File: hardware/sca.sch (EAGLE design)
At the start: 45 parts, among them Q1 BSS138, Q2 BSS138, U1 MIC5225-3.3, U5 FGPMMOPA6H, U6 MIC5225-3.3, Y1 32.768kHz

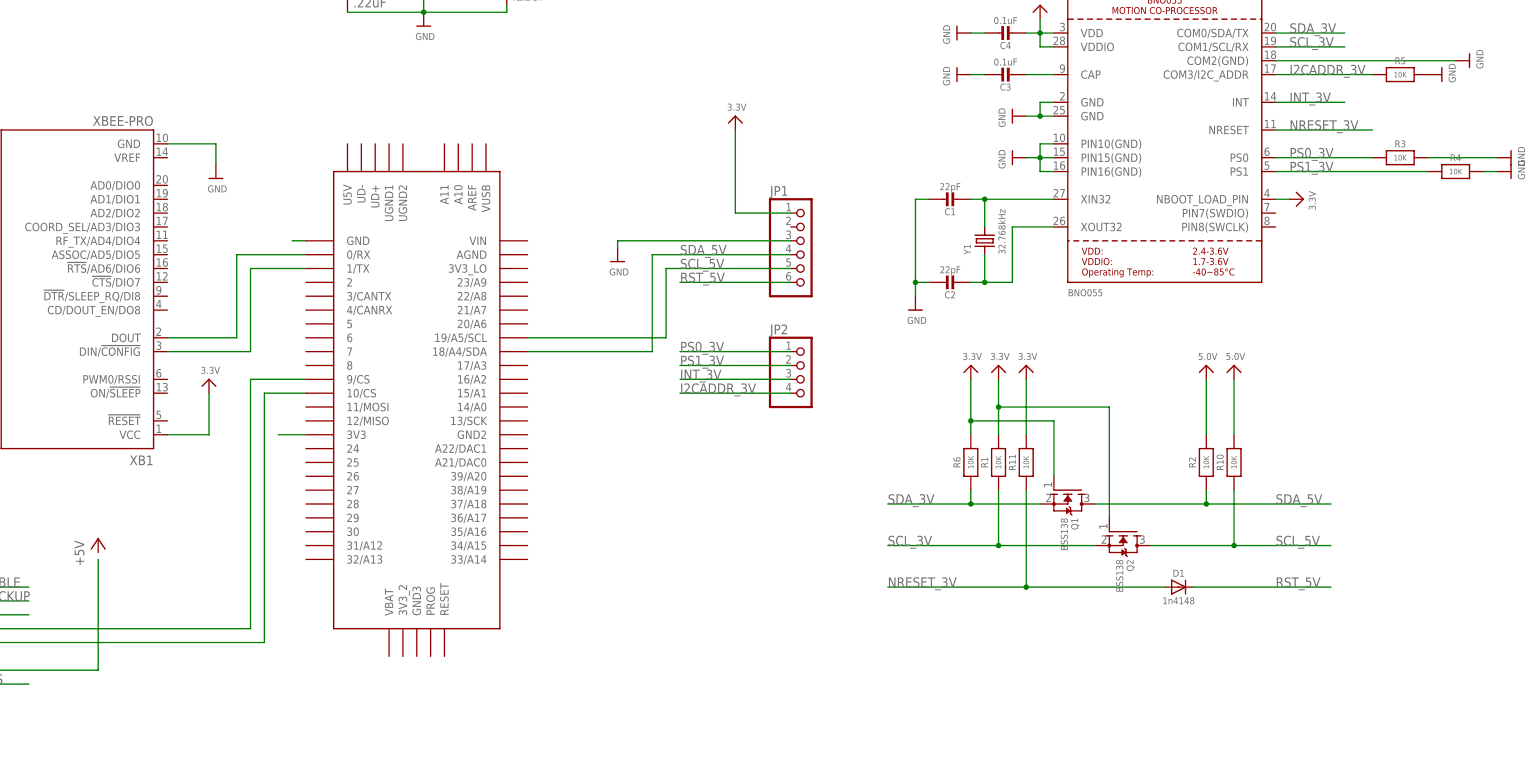
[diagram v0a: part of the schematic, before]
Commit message: Added 4x photoresistors
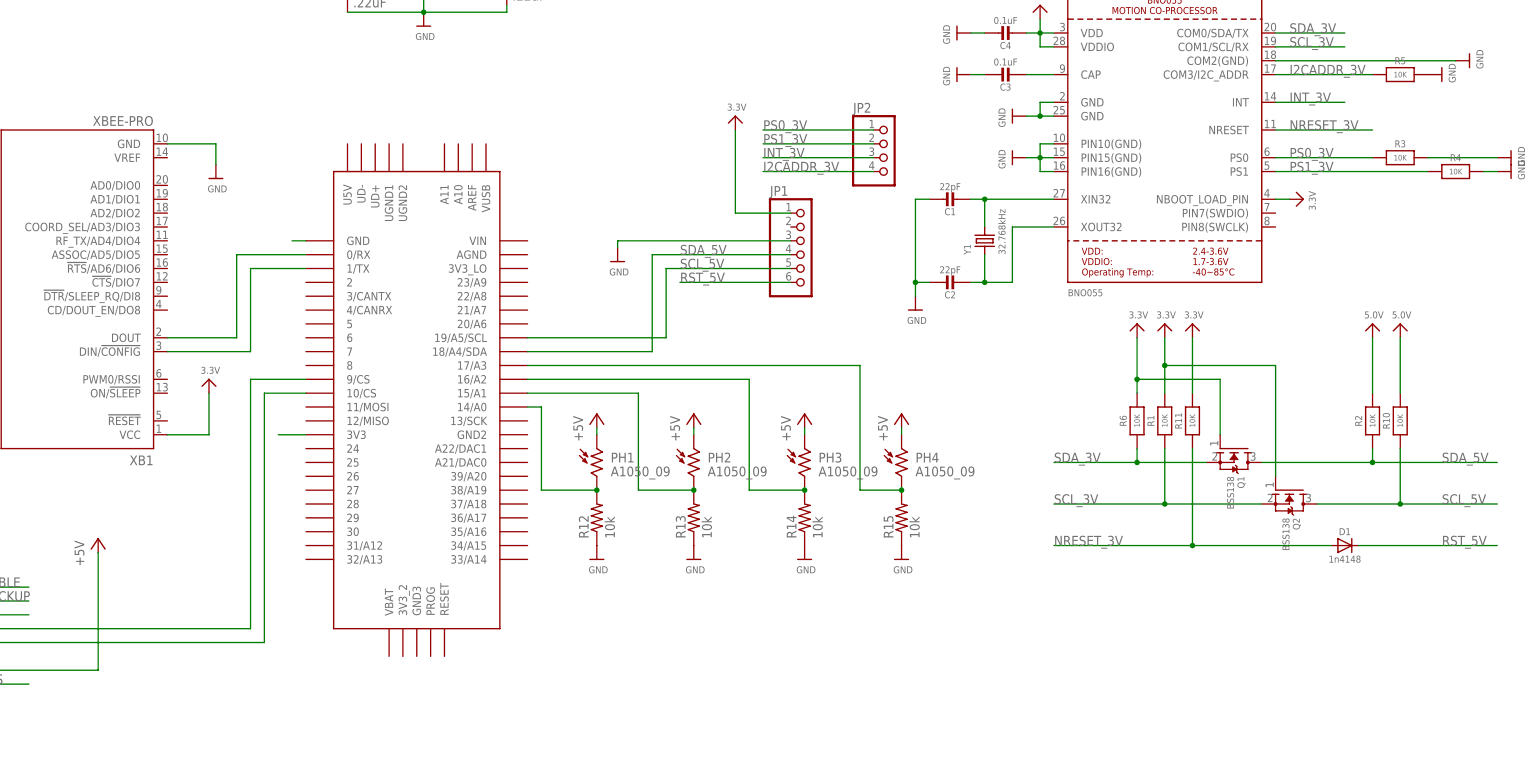
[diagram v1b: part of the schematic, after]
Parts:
- added PH1, PH2, PH3, PH4: A1050_09, photo-elements:A1050_09
- added R12, R13, R14, R15: 10k, adafruit:R-US_0204/2V
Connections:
- new net N$10: PH2.2, R13.2, U$1.15/A1
- new net N$11: PH3.2, R14.2, U$1.16/A2
- new net N$12: PH4.2, R15.2, U$1.17/A3
- net +5V: now also JP3.2, PH1.1, PH2.1, PH3.1, PH4.1
- net GND: now also R12.1, R13.1, R14.1, R15.1
- net N$5: now also PH1.2, R12.2, U$1.14/A0; no longer JP3.2
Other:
- moved on the sheet: D1, JP2, Q1, Q2, R1, R10, R11, R2, R6

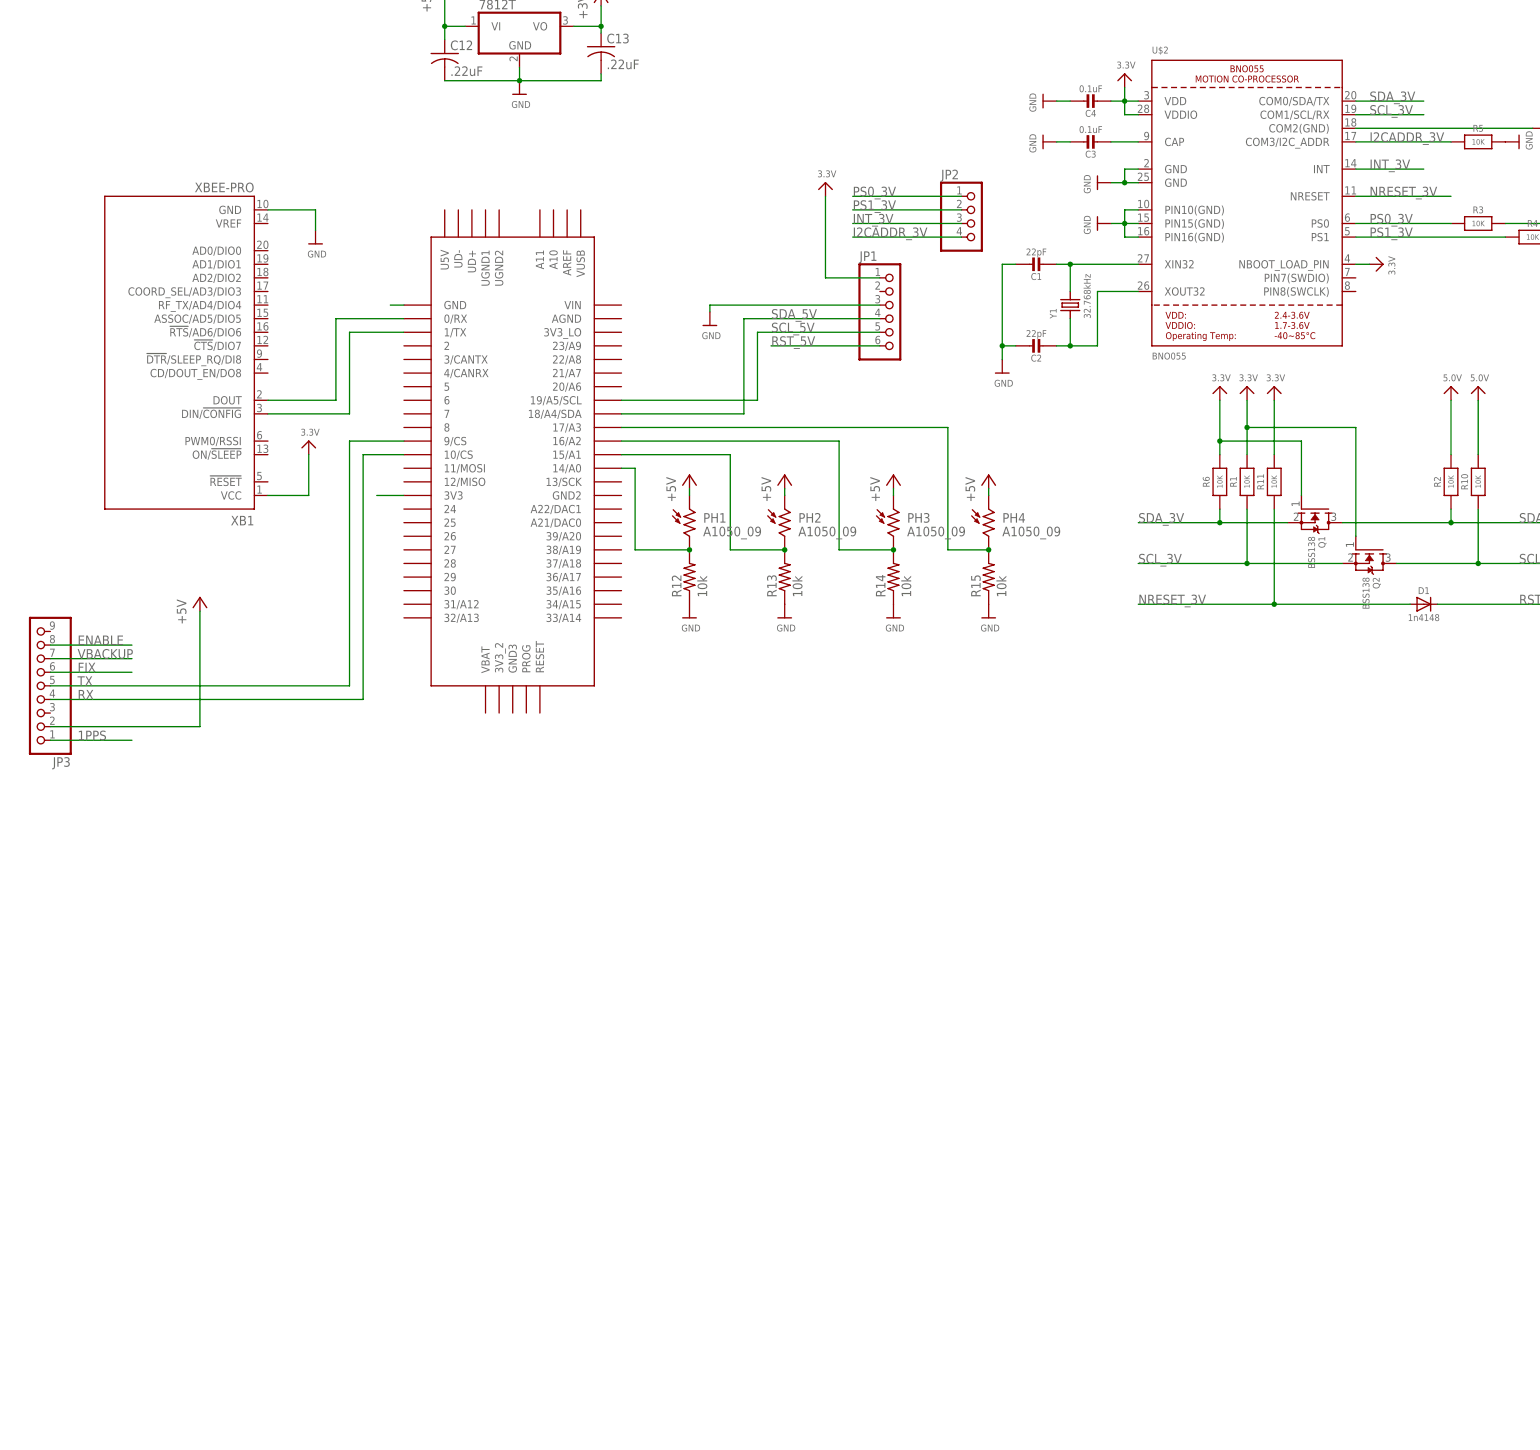
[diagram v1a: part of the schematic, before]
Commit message: Added bmp388
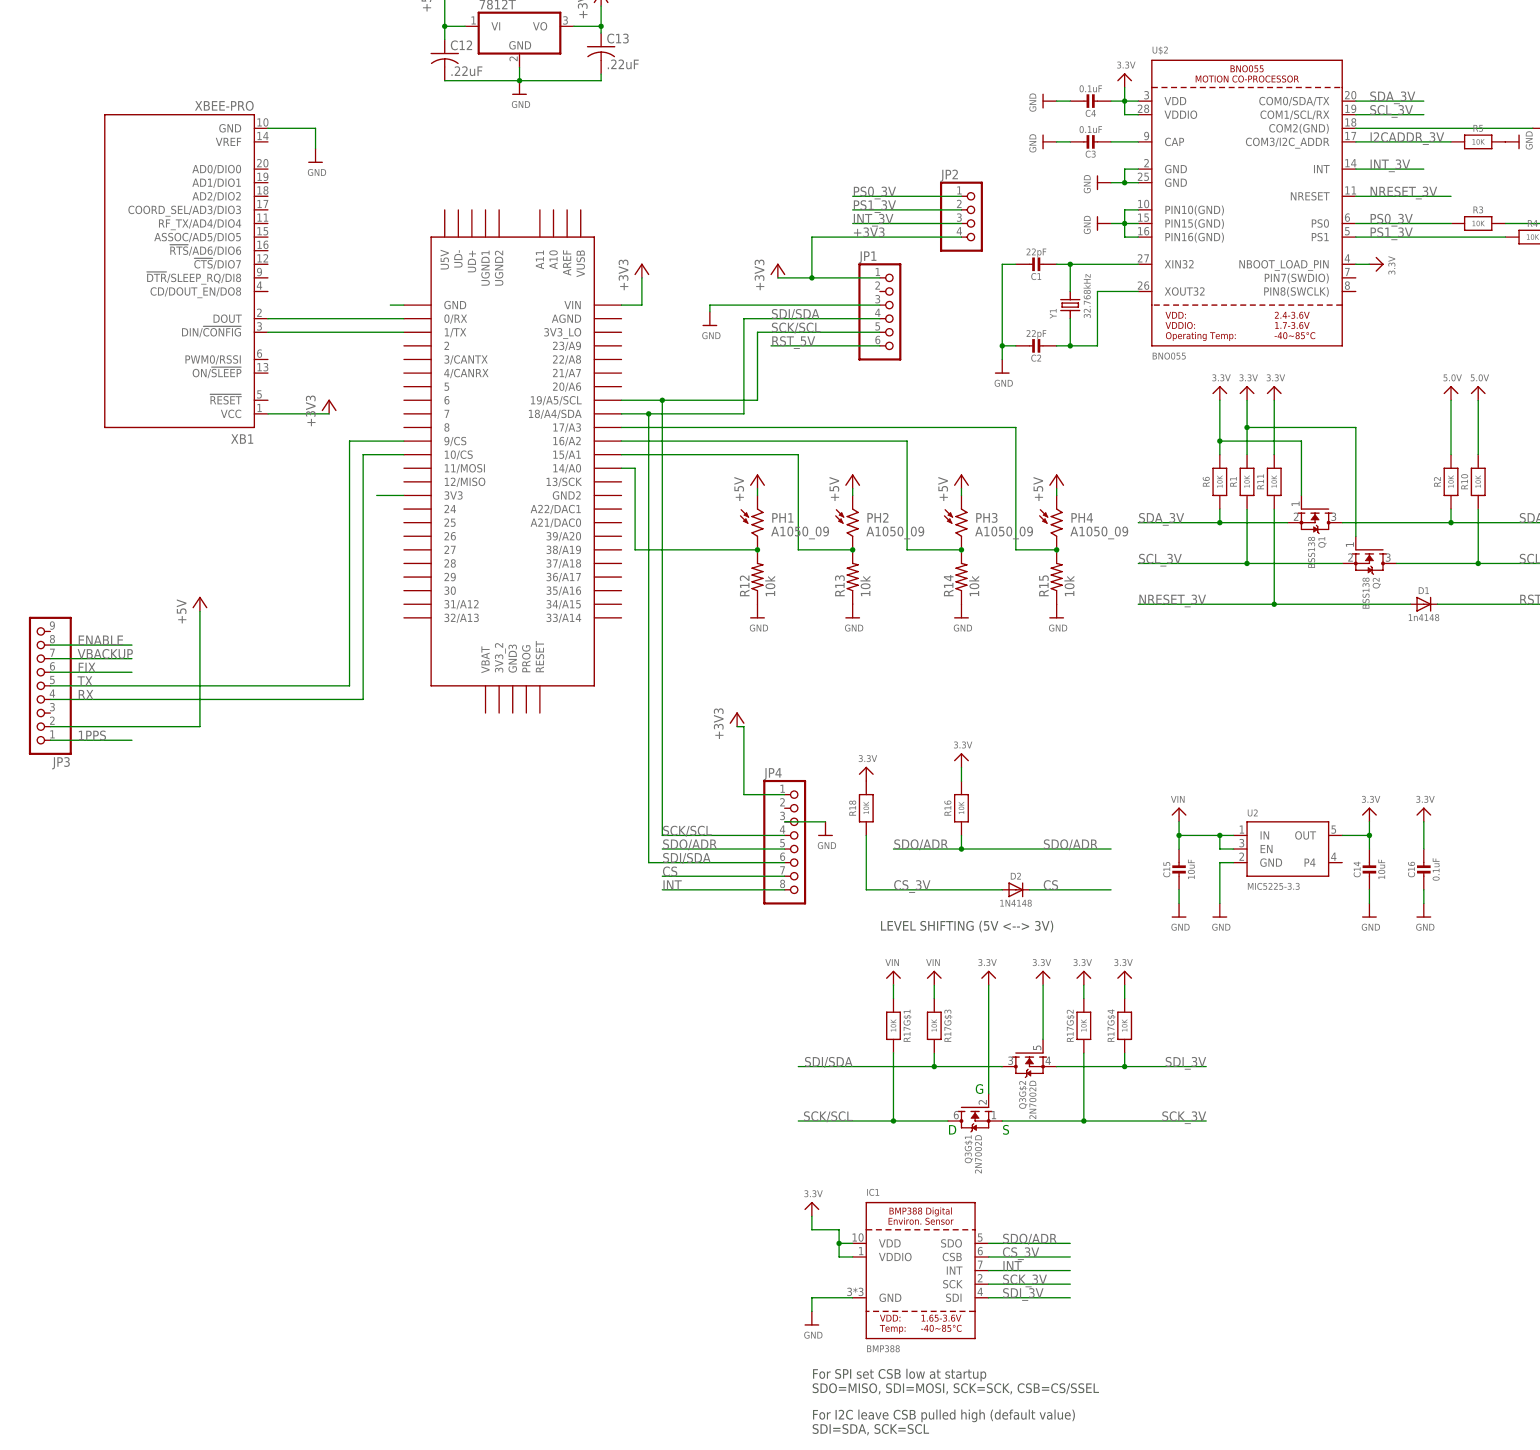
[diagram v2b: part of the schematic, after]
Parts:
- added C14, C15: 10uF, microbuilder:CAP_CERAMIC0805-NOOUTLINE
- added C16: 0.1uF, microbuilder:CAP_CERAMIC0603_NO
- added D2: 1N4148, microbuilder:DIODESOD-323
- added IC1: BMP388, microbuilder:BMP388
- added JP4: (no value), microbuilder:HEADER-1X870MIL
- added Q3: 2N7002D, microbuilder:MOSFET-N_DUAL
- added R16, R18: 10K, microbuilder:RESISTOR_0603_NOOUT
- added R17: 10K, microbuilder:RESISTOR_4PACK
- added U2: MIC5225-3.3, microbuilder:VREG_SOT23-5
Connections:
- new net CS: D2.C, JP4.7
- new net CS_3V: D2.A, IC1.CSB, R18.1
- new net INT: IC1.INT, JP4.8
- new net SCK/SCL: JP1.5, JP4.4, Q3G$1.D, R17G$1.2, U$1.19/A5/SCL
- new net SCK_3V: IC1.SCK, Q3G$1.S, R17G$2.2
- new net SDI/SDA: JP1.4, JP4.6, Q3G$2.D, R17G$3.2, U$1.18/A4/SDA
- new net SDI_3V: IC1.SDI, Q3G$2.S, R17G$4.2
- new net SDO/ADR: IC1.SDO, JP4.5, R16.1
- net +3V3: now also JP1.1, JP2.4, JP4.1, U$1.VIN, XB1.VCC
- net 3.3V: now also C14.1, C16.1, IC1.VDD, IC1.VDDIO, Q3G$1.G, Q3G$2.G, R16.2, R17G$2.1, R17G$4.1, R18.2, U2.OUT; no longer JP1.1, XB1.VCC
- net GND: now also C14.2, C15.2, C16.2, IC1.GND, JP4.3, U2.GND
- net I2CADDR_3V: no longer JP2.4
- net SCL_5V: no longer JP1.5, U$1.19/A5/SCL
- net SDA_5V: no longer JP1.4, U$1.18/A4/SDA
- net VIN: now also C15.1, R17G$1.1, R17G$3.1, U2.EN, U2.IN
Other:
- note added: "D"
- note added: "For I2C leave CSB pulled high (default value) SDI=SDA, SCK=SCL"
- note added: "For SPI set CSB low at startup SDO=MISO, SDI=MOSI, SCK=SCK, CSB=CS/SSEL"
- note added: "G"
- note added: "LEVEL SHIFTING (5V <--> 3V)"
- note added: "S"
- moved on the sheet: PH1, PH2, PH3, PH4, R12, R13, R14, R15, XB1
